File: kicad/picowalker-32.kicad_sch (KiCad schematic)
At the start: 21 parts, among them IC1 TFBS4711-TT1, IC2 M95512-DRMN8TP_K, IC3 IS25WP128F-JBLE, J1 DBG_HDR, J2 PROGRAM_HDR, SW1 SW_Push, SW2 SW_Push, SW3 SW_Push, U3 BMA400

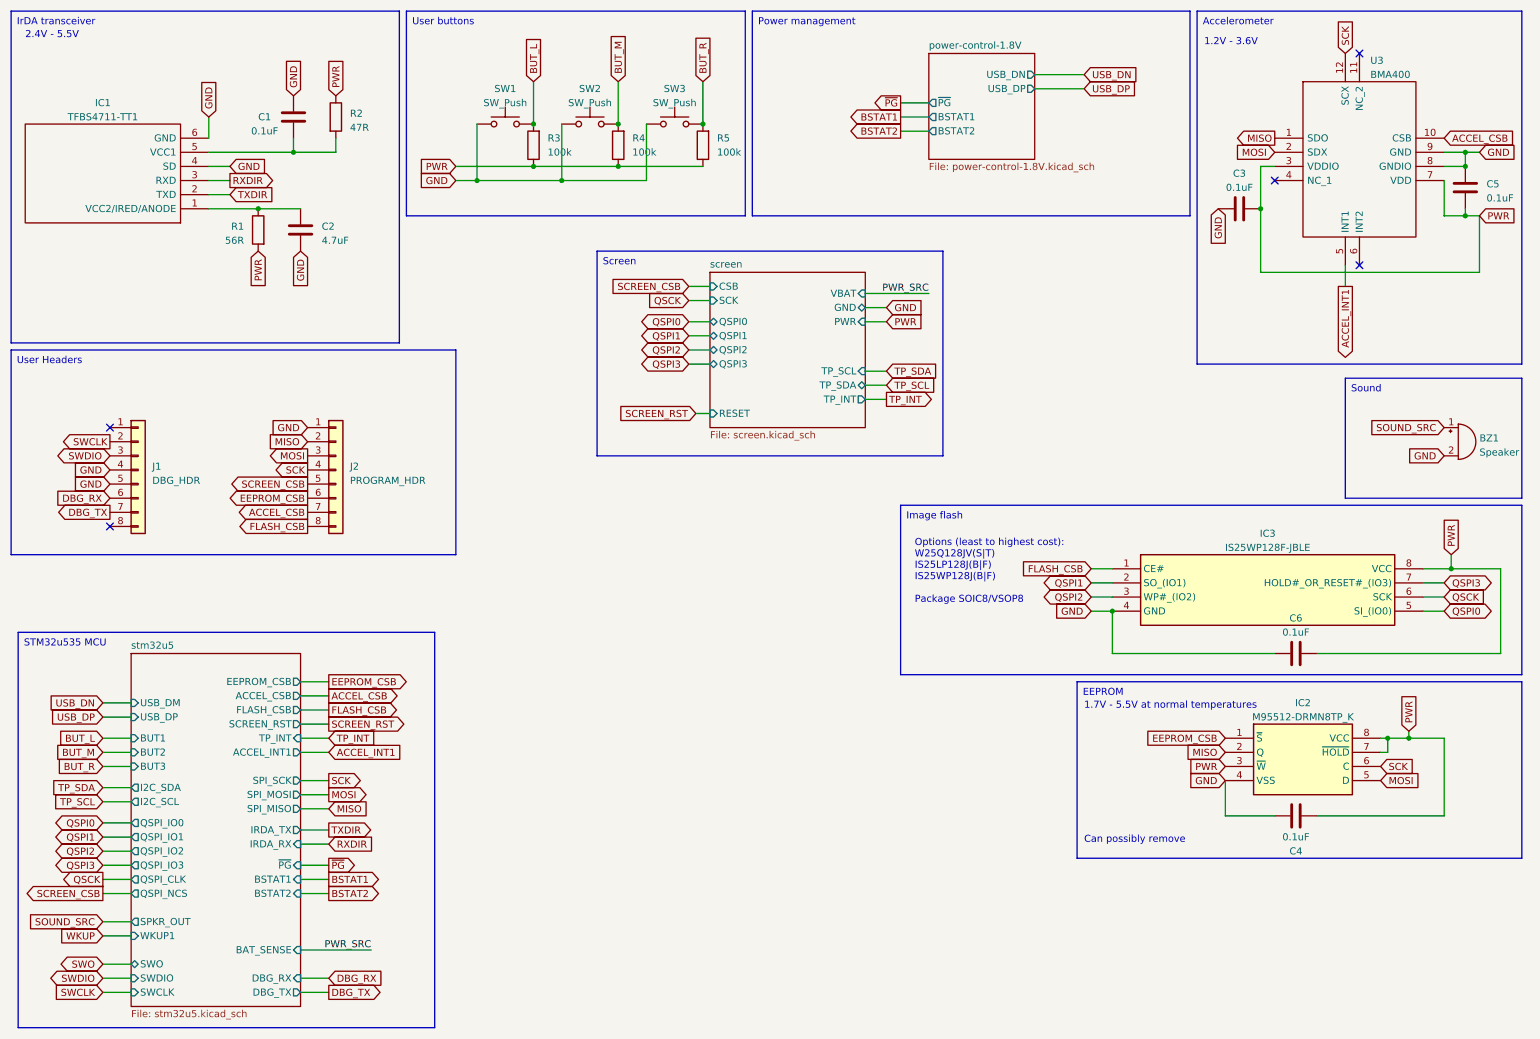
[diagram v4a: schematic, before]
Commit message: hw: change to 3v3 LDO and remove unnecessary MCU pins
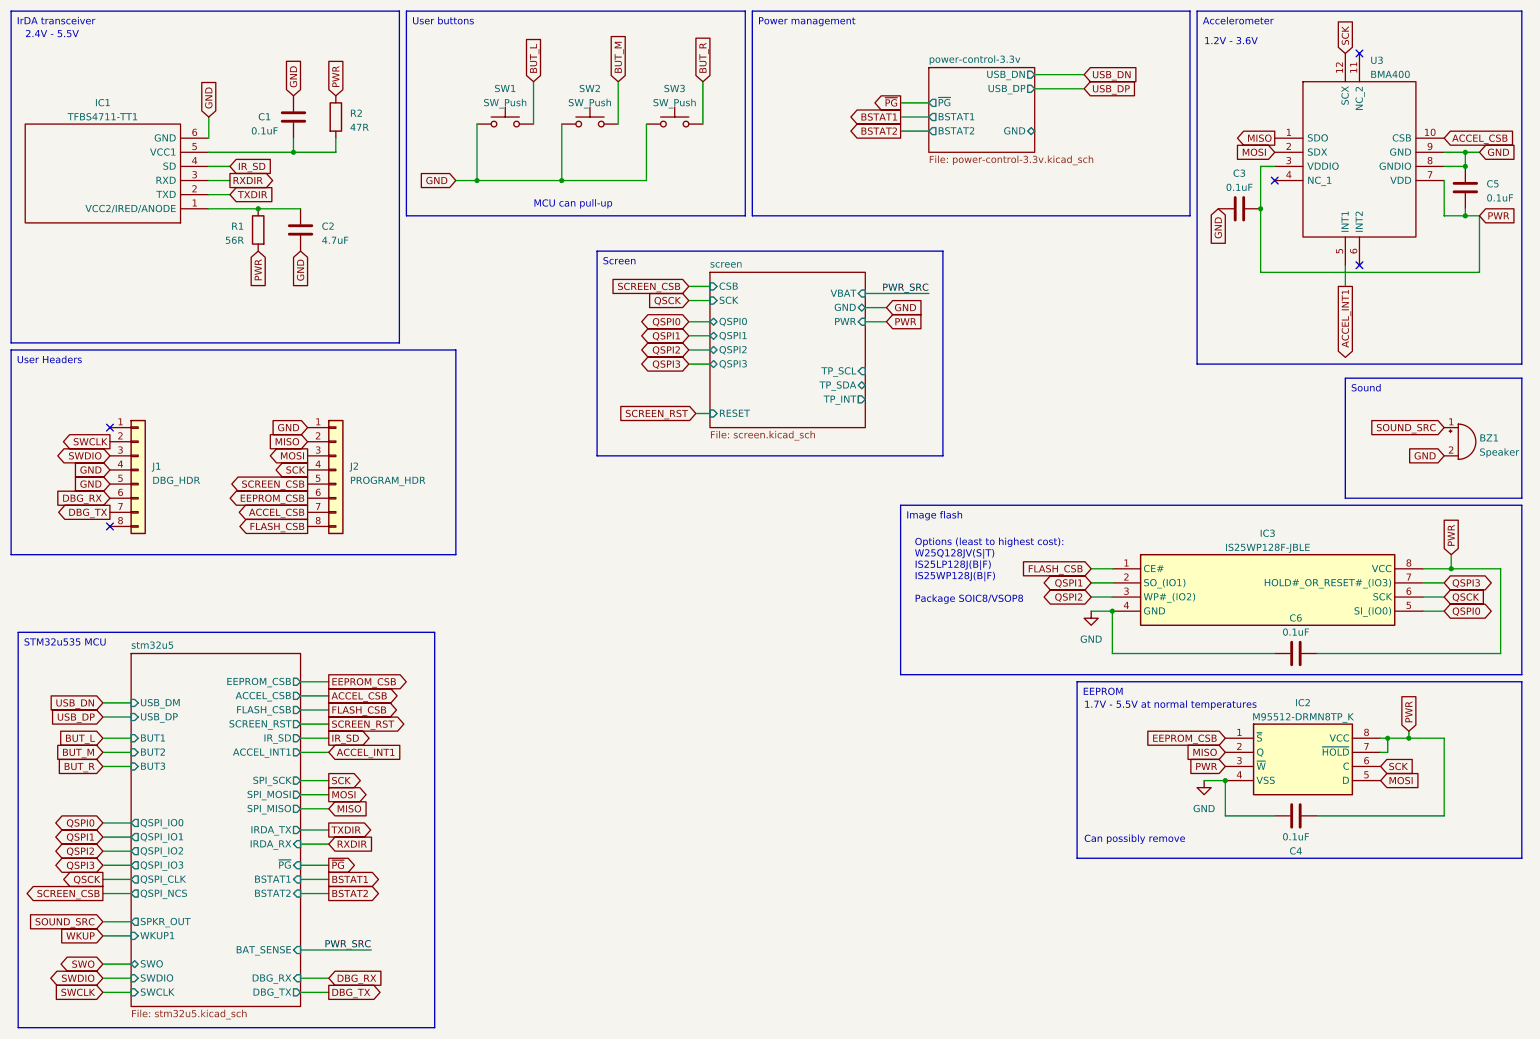
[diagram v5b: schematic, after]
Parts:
- removed R3, R4, R5: 100k, Resistor_SMD:R_0402_1005Metric, symbol Device:R
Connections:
- net GND: no longer IC1.4 (SD)
- new net IR_SD: IC1.4 (SD)
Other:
- removed sheet power-control-1.8V
- added sheet power-control-3.3v (power-control-3.3v.kicad_sch)
- sheet stm32u5 ports: added IR_SD; removed I2C_SCL, I2C_SDA, TP_INT
- note added: "MCU can pull-up"

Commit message: hw: update power symbols, clean up some power circuitry
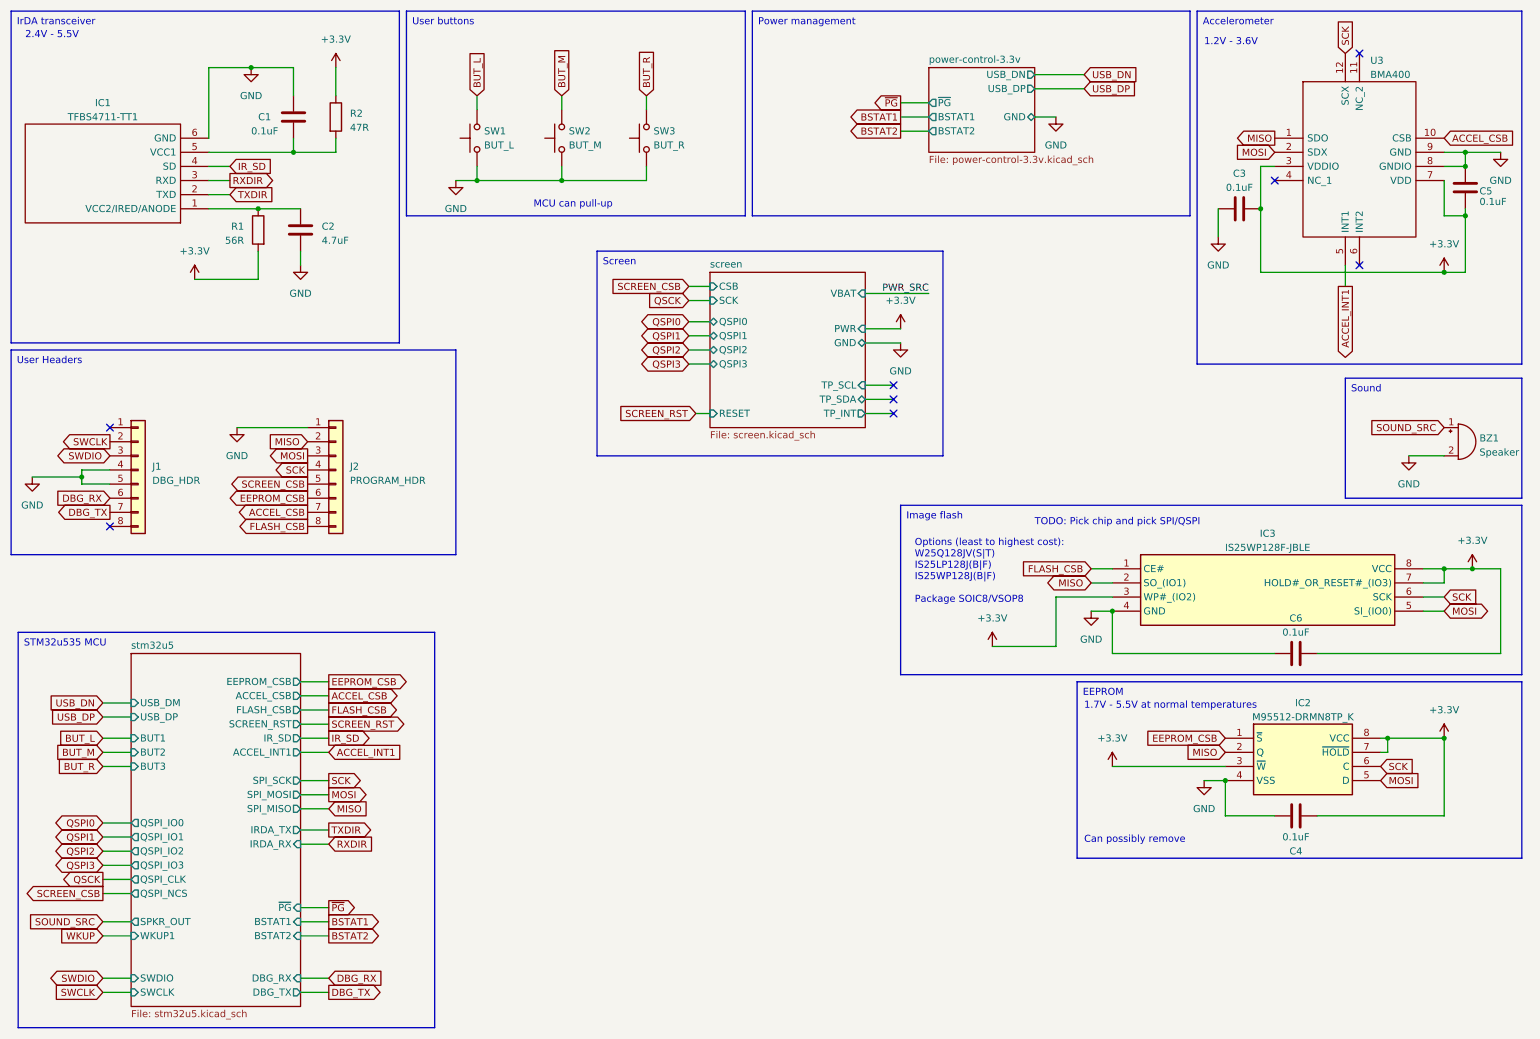
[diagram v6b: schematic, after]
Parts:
- SW1: value SW_Push -> BUT_L
- SW2: value SW_Push -> BUT_M
- SW3: value SW_Push -> BUT_R
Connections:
- net MISO: now also IC3.2 (SO_(IO1))
- net MOSI: now also IC3.5 (SI_(IO0))
- net QSCK: no longer IC3.6 (SCK)
- net QSPI0: no longer IC3.5 (SI_(IO0))
- net QSPI1: no longer IC3.2 (SO_(IO1))
- net QSPI2: no longer IC3.3 (WP#_(IO2))
- net QSPI3: no longer IC3.7 (HOLD#_OR_RESET#_(IO3))
- net SCK: now also IC3.6 (SCK)
- net PWR renamed +3.3V
- net +3.3V: now also IC3.3 (WP#_(IO2)), IC3.7 (HOLD#_OR_RESET#_(IO3))
- no-connect marks 5 -> 8
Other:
- sheet stm32u5 ports: added none; removed BAT_SENSE, SWO
- note added: "TODO: Pick chip and pick SPI/QSPI"
- moved on the sheet: SW1, SW2, SW3

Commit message: hw: change battery to a "simpler" version
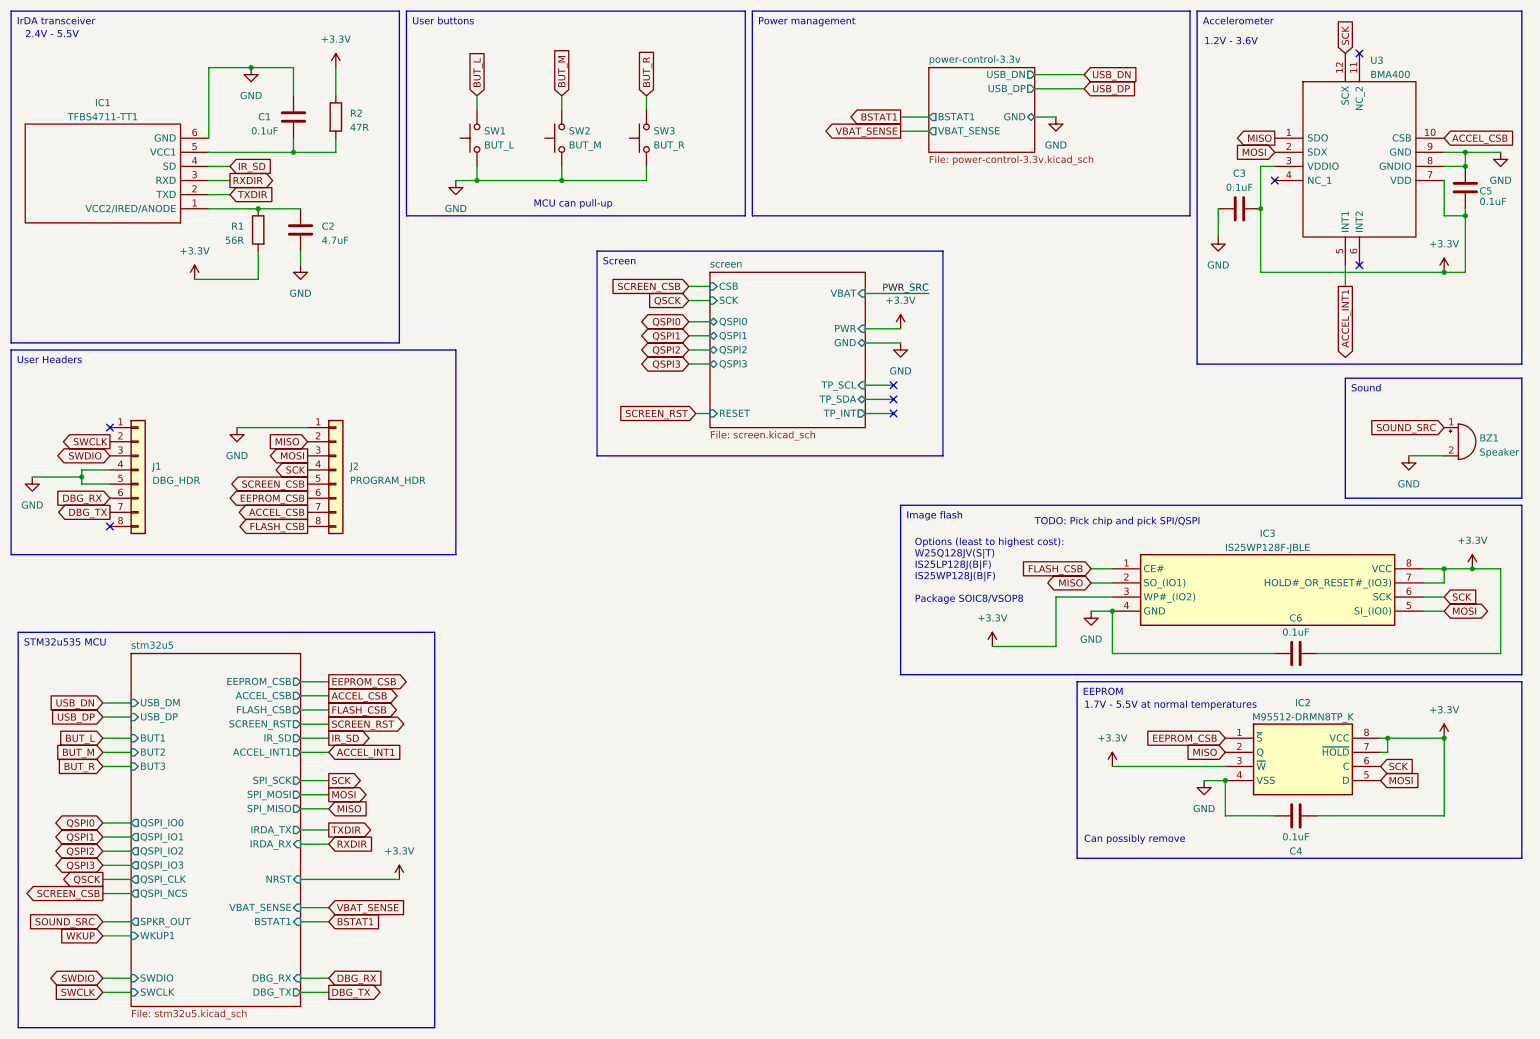
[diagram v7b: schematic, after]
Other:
- sheet power-control-3.3v ports: added VBAT_SENSE; removed BSTAT2, ~{PG}
- sheet stm32u5 ports: added NRST, VBAT_SENSE; removed BSTAT2, ~{PG}
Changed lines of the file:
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@@
+    (stroke (width 0) (type default))
+  )
+  (wire (pts (xy 172.72 34.29) (xy 177.8 34.29))
+    (stroke (width 0) (type default))
+  )
+  (wire (pts (xy 64.77 168.91) (xy 82.55 168.91))
     (stroke (width 0) (type default))
   )
@@
     (stroke (width 0) (type default))
   )
-  (wire (pts (xy 172.72 29.21) (xy 177.8 29.21))
-    (stroke (width 0) (type default))
-  )
-  (wire (pts (xy 172.72 34.29) (xy 177.8 34.29))
-    (stroke (width 0) (type default))
-  )
   (wire (pts (xy 210.82 148.59) (xy 231.14 148.59))
     (stroke (width 0) (type default))
@@
     (stroke (width 0) (type default))
   )
+  (wire (pts (xy 166.37 82.55) (xy 171.45 82.55))
+    (stroke (width 0) (type default))
+  )
+  (wire (pts (xy 127 40.64) (xy 127 43.18))
+    (stroke (width 0) (type default))
+  )
+  (wire (pts (xy 207.01 113.03) (xy 210.82 113.03))
+    (stroke (width 0) (type default))
+  )
+  (wire (pts (xy 111.76 27.94) (xy 111.76 30.48))
+    (stroke (width 0) (type default))
+  )
+  (wire (pts (xy 166.37 80.01) (xy 171.45 80.01))
+    (stroke (width 0) (type default))
+  )
+  (wire (pts (xy 64.77 189.23) (xy 69.85 189.23))
+    (stroke (width 0) (type default))
+  )
+  (wire (pts (xy 270.51 49.53) (xy 274.32 49.53))
+    (stroke (width 0) (type default))
+  )
+  (wire (pts (xy 29.21 143.51) (xy 34.29 143.51))
+    (stroke (width 0) (type default))
+  )
+  (wire (pts (xy 16.51 96.52) (xy 25.4 96.52))
+    (stroke (width 0) (type default))
+  )
+  (wire (pts (xy 25.4 96.52) (xy 25.4 97.79))
+    (stroke (width 0) (type default))
+  )
+  (wire (pts (xy 210.82 120.65) (xy 210.82 128.27))
+    (stroke (width 0) (type default))
+  )
+  (wire (pts (xy 237.49 48.26) (xy 237.49 40.64))
+    (stroke (width 0) (type default))
+  )
   (wire (pts (xy 64.77 173.99) (xy 69.85 173.99))
-    (stroke (width 0) (type default))
-  )
-  (wire (pts (xy 166.37 82.55) (xy 171.45 82.55))
-    (stroke (width 0) (type default))
-  )
-  (wire (pts (xy 127 40.64) (xy 127 43.18))
-    (stroke (width 0) (type default))
-  )
-  (wire (pts (xy 207.01 113.03) (xy 210.82 113.03))
-    (stroke (width 0) (type default))
-  )
-  (wire (pts (xy 111.76 27.94) (xy 111.76 30.48))
-    (stroke (width 0) (type default))
-  )
-  (wire (pts (xy 166.37 80.01) (xy 171.45 80.01))
-    (stroke (width 0) (type default))
-  )
-  (wire (pts (xy 64.77 189.23) (xy 69.85 189.23))
-    (stroke (width 0) (type default))
-  )
-  (wire (pts (xy 270.51 49.53) (xy 274.32 49.53))
-    (stroke (width 0) (type default))
-  )
-  (wire (pts (xy 29.21 143.51) (xy 34.29 143.51))
-    (stroke (width 0) (type default))
-  )
-  (wire (pts (xy 16.51 96.52) (xy 25.4 96.52))
-    (stroke (width 0) (type default))
-  )
-  (wire (pts (xy 64.77 179.07) (xy 69.85 179.07))
-    (stroke (width 0) (type default))
-  )
-  (wire (pts (xy 25.4 96.52) (xy 25.4 97.79))
-    (stroke (width 0) (type default))
-  )
-  (wire (pts (xy 210.82 120.65) (xy 210.82 128.27))
-    (stroke (width 0) (type default))
-  )
-  (wire (pts (xy 237.49 48.26) (xy 237.49 40.64))
     (stroke (width 0) (type default))
   )
@@
     )
   )
-  (global_label "BSTAT2" (shape output) (at 69.85 179.07 0) (fields_autoplaced)
-    (effects (font (size 1.27 1.27)) (justify left))
-    (property "Intersheetrefs" "${INTERSHEET_REFS}" (at 79.548 179.07 0)
-      (effects (font (size 1.27 1.27)) (justify left) hide)
-    )
-  )
   (global_label "RXDIR" (shape output) (at 52.07 43.18 0) (fields_autoplaced)
     (effects (font (size 1.27 1.27)) (justify left))
@@
     )
   )
-  (global_label "~{PG}" (shape output) (at 172.72 29.21 180) (fields_autoplaced)
-    (effects (font (size 1.27 1.27)) (justify right))
-    (property "Intersheetrefs" "${INTERSHEET_REFS}" (at 167.1948 29.21 0)
-      (effects (font (size 1.27 1.27)) (justify right) hide)
-    )
-  )
   (global_label "FLASH_CSB" (shape output) (at 66.04 105.41 180) (fields_autoplaced)
     (effects (font (size 1.27 1.27)) (justify right))
@@
     )
   )
+  (global_label "VBAT_SENSE" (shape input) (at 69.85 173.99 0) (fields_autoplaced)
+    (effects (font (size 1.27 1.27)) (justify left))
+    (property "Intersheetrefs" "${INTERSHEET_REFS}" (at 84.2651 173.99 0)
+      (effects (font (size 1.27 1.27)) (justify left) hide)
+    )
+  )
   (global_label "SCREEN_RST" (shape output) (at 69.85 140.97 0) (fields_autoplaced)
     (effects (font (size 1.27 1.27)) (justify left))
@@
     )
   )
-  (global_label "BSTAT1" (shape output) (at 69.85 176.53 0) (fields_autoplaced)
+  (global_label "BSTAT1" (shape input) (at 69.85 176.53 0) (fields_autoplaced)
     (effects (font (size 1.27 1.27)) (justify left))
     (property "Intersheetrefs" "${INTERSHEET_REFS}" (at 79.548 176.53 0)
@@
     )
   )
-  (global_label "~{PG}" (shape output) (at 69.85 173.99 0) (fields_autoplaced)
-    (effects (font (size 1.27 1.27)) (justify left))
-    (property "Intersheetrefs" "${INTERSHEET_REFS}" (at 75.3752 173.99 0)
-      (effects (font (size 1.27 1.27)) (justify left) hide)
-    )
-  )
   (global_label "SWCLK" (shape output) (at 30.48 90.17 180) (fields_autoplaced)
     (effects (font (size 1.27 1.27)) (justify right))
@@
     )
   )
+  (global_label "VBAT_SENSE" (shape output) (at 172.72 34.29 180) (fields_autoplaced)
+    (effects (font (size 1.27 1.27)) (justify right))
+    (property "Intersheetrefs" "${INTERSHEET_REFS}" (at 158.3049 34.29 0)
+      (effects (font (size 1.27 1.27)) (justify right) hide)
+    )
+  )
   (global_label "MOSI" (shape input) (at 259.08 151.13 0) (fields_autoplaced)
     (effects (font (size 1.27 1.27)) (justify left))
@@
     )
   )
-  (global_label "BSTAT2" (shape output) (at 172.72 34.29 180) (fields_autoplaced)
-    (effects (font (size 1.27 1.27)) (justify right))
-    (property "Intersheetrefs" "${INTERSHEET_REFS}" (at 163.022 34.29 0)
-      (effects (font (size 1.27 1.27)) (justify right) hide)
-    )
-  )
   (global_label "SCK" (shape input) (at 270.51 118.11 0) (fields_autoplaced)
     (effects (font (size 1.27 1.27)) (justify left))
@@
         (path "/17fa99ff-0271-4e85-b8d9-a0357d961230"
           (reference "#PWR02") (unit 1)
+        )
+      )
+    )
+  )
+  (symbol (lib_id "power:+3.3V") (at 82.55 168.91 0) (unit 1)
+    (in_bom yes) (on_board yes) (dnp no) (fields_autoplaced)
+    (property "Reference" "#PWR023" (at 82.55 172.72 0)
+      (effects (font (size 1.27 1.27)) hide)
+    )
+    (property "Value" "+3.3V" (at 82.55 163.83 0)
+      (effects (font (size 1.27 1.27)))
+    )
+    (property "Footprint" "" (at 82.55 168.91 0)
+      (effects (font (size 1.27 1.27)) hide)
+    )
+    (property "Datasheet" "" (at 82.55 168.91 0)
+      (effects (font (size 1.27 1.27)) hide)
+    )
+    (pin "1")
+    (instances
+      (project "picowalker-32"
+        (path "/17fa99ff-0271-4e85-b8d9-a0357d961230"
+          (reference "#PWR023") (unit 1)
         )
       )
@@
       (effects (font (size 1.27 1.27)) (justify right))
     )
-    (pin "~{PG}" input (at 64.77 173.99 0)
-      (effects (font (size 1.27 1.27)) (justify right))
-    )
     (pin "BSTAT1" input (at 64.77 176.53 0)
       (effects (font (size 1.27 1.27)) (justify right))
     )
-    (pin "BSTAT2" input (at 64.77 179.07 0)
-      (effects (font (size 1.27 1.27)) (justify right))
-    )
     (pin "IR_SD" output (at 64.77 143.51 0)
+      (effects (font (size 1.27 1.27)) (justify right))
+    )
+    (pin "NRST" input (at 64.77 168.91 0)
+      (effects (font (size 1.27 1.27)) (justify right))
+    )
+    (pin "VBAT_SENSE" input (at 64.77 173.99 0)
       (effects (font (size 1.27 1.27)) (justify right))
     )
@@
       (effects (font (size 1.27 1.27)) (justify right))
     )
-    (pin "~{PG}" output (at 177.8 29.21 180)
-      (effects (font (size 1.27 1.27)) (justify left))
-    )
     (pin "USB_DP" output (at 196.85 26.67 0)
       (effects (font (size 1.27 1.27)) (justify right))
@@
       (effects (font (size 1.27 1.27)) (justify right))
     )
-    (pin "BSTAT2" output (at 177.8 34.29 180)
-      (effects (font (size 1.27 1.27)) (justify left))
-    )
     (pin "BSTAT1" output (at 177.8 31.75 180)
       (effects (font (size 1.27 1.27)) (justify left))
     )
+    (pin "VBAT_SENSE" output (at 177.8 34.29 180)
+      (effects (font (size 1.27 1.27)) (justify left))
+    )
